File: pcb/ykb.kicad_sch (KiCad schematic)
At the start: 42 parts

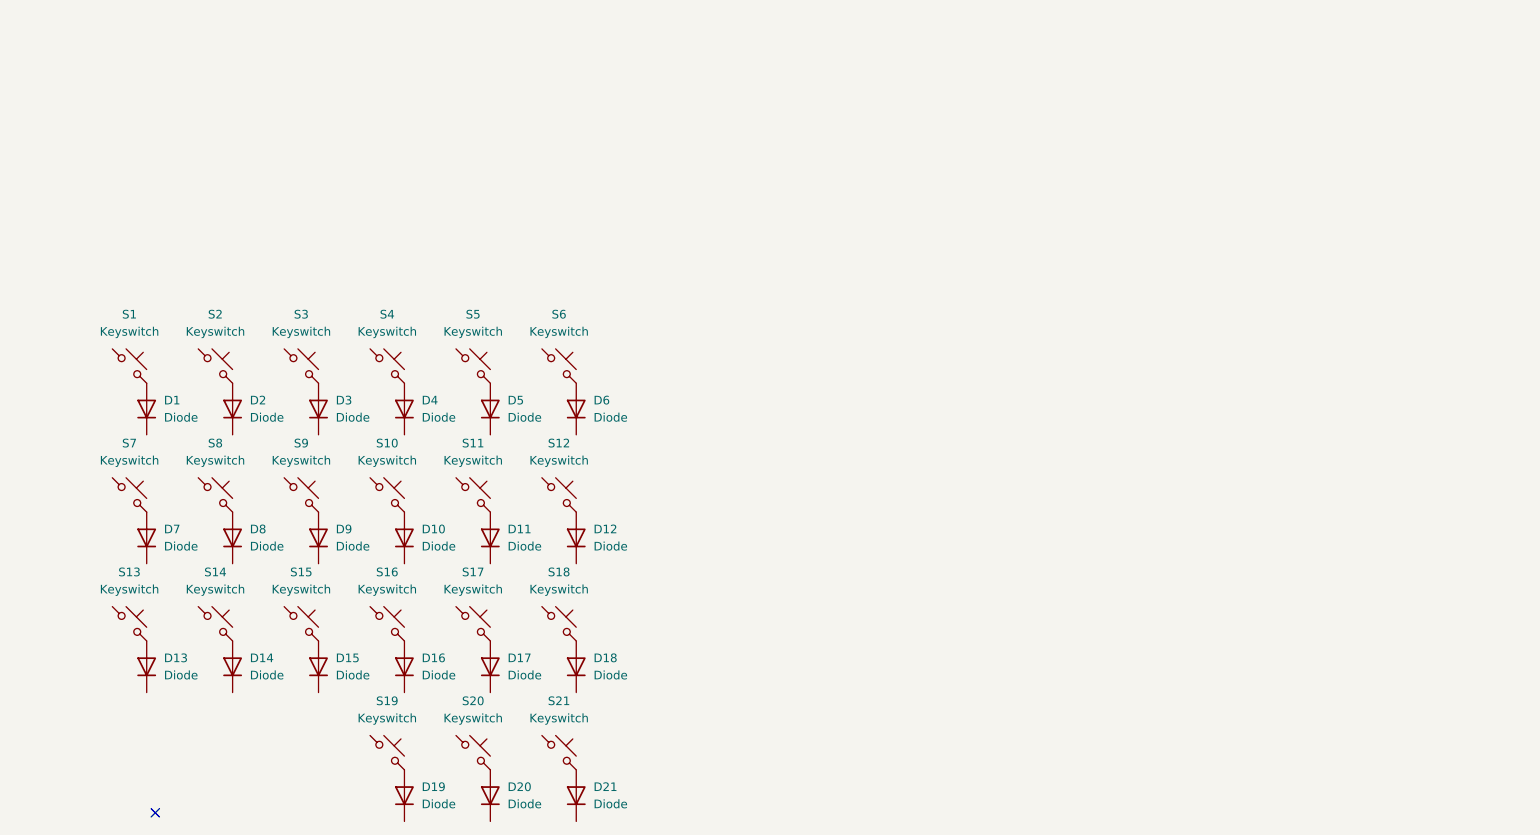
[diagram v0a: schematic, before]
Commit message: proper footprints and s/d connections made
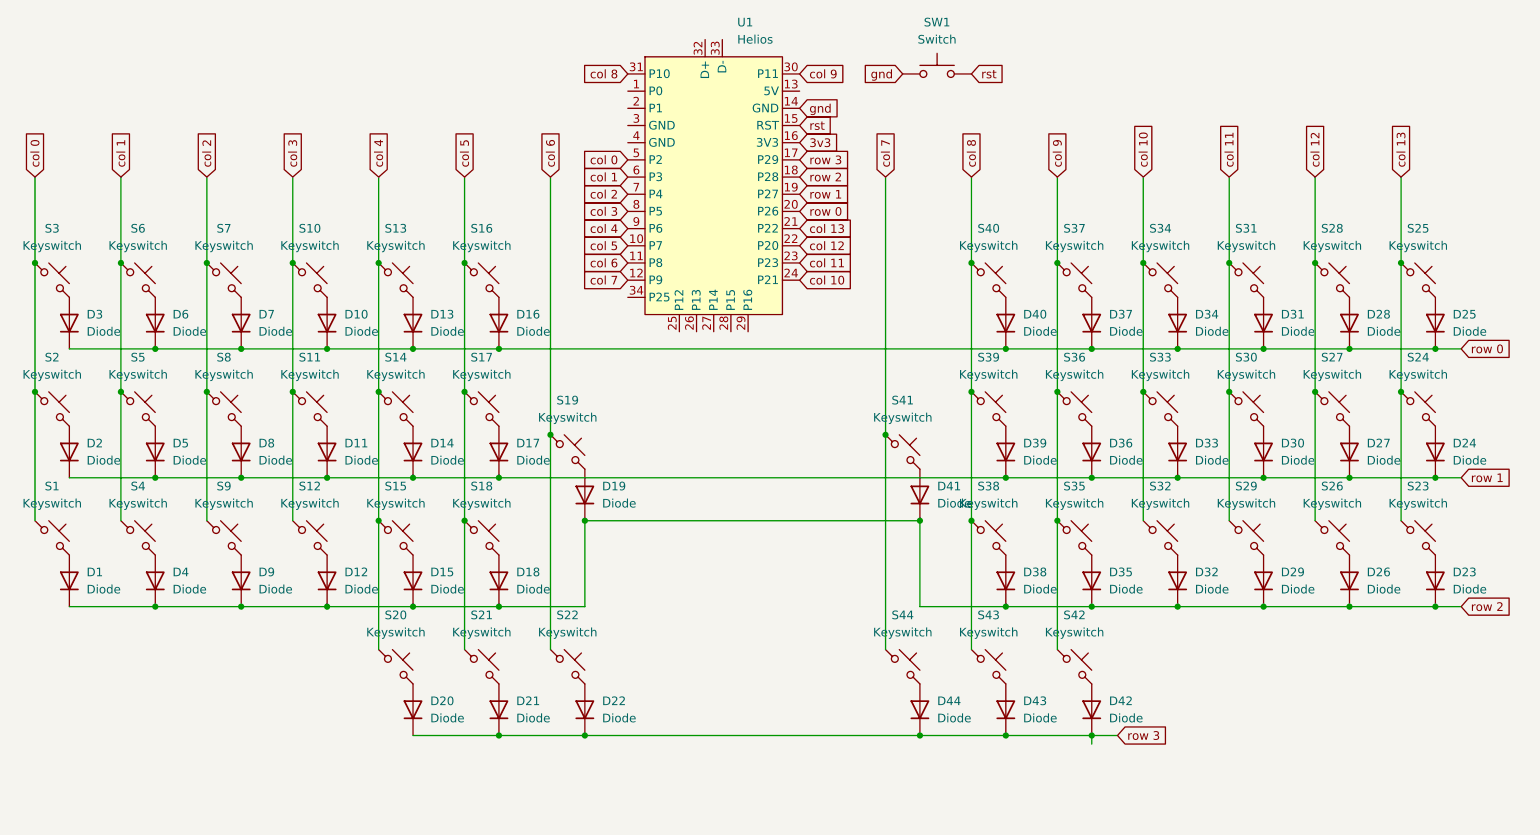
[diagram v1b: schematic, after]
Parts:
- added D22, D23, D24, D25, D26, D27, D28, D29, D30, D31, D32, D33, D34, D35, D36, D37, D38, D39, D40, D41, D42, D43, D44: Diode, ScottoKeebs_Components:Diode_SOD-123, symbol ScottoKeebs:Placeholder_Diode
- added S22, S23, S24, S25, S26, S27, S28, S29, S30, S31, S32, S33, S34, S35, S36, S37, S38, S39, S40, S41, S42, S43, S44: Keyswitch, ScottoKeebs_Hotswap:Hotswap_Choc_V1V2_1.00u, symbol ScottoKeebs:Placeholder_Keyswitch
- added SW1: Switch, ScottoKeebs_Components:Switch_MSK12C02, symbol ScottoKeebs:Placeholder_Switch
- added U1: Helios, PCM_marbastlib-xp-promicroish:Helios_AH_USBup, symbol PCM_marbastlib-promicroish:Helios
- D1, D10, D11, D12, D13, D14, D15, D16, D17, D18, D19, D2, D20, D21, D3, D4, D5, D6, D7, D8, D9: footprint (none) -> ScottoKeebs_Components:Diode_SOD-123
- S1, S10, S11, S12, S13, S14, S15, S16, S17, S18, S19, S2, S20, S21, S3, S4, S5, S6, S7, S8, S9: footprint (none) -> ScottoKeebs_Hotswap:Hotswap_Choc_V1V2_1.00u
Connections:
- net row 0: now reaches D7.1 (K)
- net row 0: now also D10.1 (K), D13.1 (K), D16.1 (K), D3.1 (K), D6.1 (K), D25.1 (K), D28.1 (K), D31.1 (K), D34.1 (K), D37.1 (K), D40.1 (K), U1.20 (P26)
- net col 3: now reaches S10.1
- net col 3: now also S11.1, S12.1, U1.8 (P5)
- net row 1: now reaches D14.1 (K)
- net row 1: now also D11.1 (K), D17.1 (K), D2.1 (K), D5.1 (K), D8.1 (K), D24.1 (K), D27.1 (K), D30.1 (K), D33.1 (K), D36.1 (K), D39.1 (K), U1.19 (P27)
- net row 2: now reaches D12.1 (K)
- net row 2: now also D1.1 (K), D15.1 (K), D18.1 (K), D19.1 (K), D4.1 (K), D9.1 (K), D23.1 (K), D26.1 (K), D29.1 (K), D32.1 (K), D35.1 (K), D38.1 (K), D41.1 (K), U1.18 (P28)
- net col 1: now reaches S6.1
- net col 1: now also S4.1, S5.1, U1.6 (P3)
- net col 6: now reaches S19.1
- net col 6: now also S22.1, U1.11 (P8)
- net col 2: now reaches S9.1
- net col 2: now also S7.1, S8.1, U1.7 (P4)
- net col 4: now reaches S15.1
- net col 4: now also S13.1, S14.1, S20.1, U1.9 (P6)
- net col 5: now reaches S17.1
- net col 5: now also S16.1, S18.1, S21.1, U1.10 (P7)
- net col 0: now reaches S1.1
- net col 0: now also S2.1, S3.1, U1.5 (P2)
- net row 3: now reaches D20.1 (K)
- net row 3: now also D21.1 (K), D22.1 (K), D42.1 (K), D43.1 (K), D44.1 (K), U1.17 (P29)
- new net: D23.2 (A), S23.2
- new net: D31.2 (A), S31.2
- new net: D39.2 (A), S39.2
- new net: D27.2 (A), S27.2
- new net: D41.2 (A), S41.2
- new net: D32.2 (A), S32.2
- new net: D36.2 (A), S36.2
- new net: D35.2 (A), S35.2
- new net: D28.2 (A), S28.2
- new net: D44.2 (A), S44.2
- new net: D38.2 (A), S38.2
- new net: D37.2 (A), S37.2
- new net: D22.2 (A), S22.2
- new net: D29.2 (A), S29.2
- new net: D40.2 (A), S40.2
- new net: D34.2 (A), S34.2
- new net: D42.2 (A), S42.2
- new net: D26.2 (A), S26.2
- new net: D24.2 (A), S24.2
- new net: D33.2 (A), S33.2
- new net: D25.2 (A), S25.2
- new net: D30.2 (A), S30.2
- new net: D43.2 (A), S43.2
- new net 3v3: U1.16 (3V3)
- new net col 10: S32.1, S33.1, S34.1, U1.24 (P21)
- new net col 11: S29.1, S30.1, S31.1, U1.23 (P23)
- new net col 12: S26.1, S27.1, S28.1, U1.22 (P20)
- new net col 13: S23.1, S24.1, S25.1, U1.21 (P22)
- new net col 7: S41.1, S44.1, U1.12 (P9)
- new net col 8: S38.1, S39.1, S40.1, S43.1, U1.31 (P10)
- new net col 9: S35.1, S36.1, S37.1, S42.1, U1.30 (P11)
- new net gnd: SW1.1, U1.14 (GND)
- new net rst: SW1.2, U1.15 (RST)
- no-connect marks 1 -> 0

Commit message: switched to castlated controller :3
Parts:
- U1: footprint PCM_marbastlib-xp-promicroish:Helios_AH_USBup -> PCM_marbastlib-xp-promicroish:Helios_AC
- renumbered D12 to D10, D10 to D12, D15 to D13, D13 to D15, D18 to D16, D16 to D18, D9 to D7, D7 to D9, S12 to S10, S10 to S12, S15 to S13, S13 to S15, S18 to S16, S16 to S18, S9 to S7, S7 to S9
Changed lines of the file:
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@@
 		(dnp no)
 		(fields_autoplaced yes)
-		(property "Reference" "S9"
+		(property "Reference" "S7"
 			(at 80.01 83.82 0)
 			(effects
@@
 			(project "ykb"
 				(path "/a72c5318-822d-41b0-b45a-b1b0853d4f62"
-					(reference "S9")
+					(reference "S7")
 					(unit 1)
 				)
@@
 		(dnp no)
 		(fields_autoplaced yes)
-		(property "Reference" "D7"
+		(property "Reference" "D9"
 			(at 85.09 58.4199 90)
 			(effects
@@
 			(project "ykb"
 				(path "/a72c5318-822d-41b0-b45a-b1b0853d4f62"
-					(reference "D7")
+					(reference "D9")
 					(unit 1)
 				)
@@
 		(dnp no)
 		(fields_autoplaced yes)
-		(property "Reference" "S18"
+		(property "Reference" "S16"
 			(at 118.11 83.82 0)
 			(effects
@@
 			(project "ykb"
 				(path "/a72c5318-822d-41b0-b45a-b1b0853d4f62"
-					(reference "S18")
+					(reference "S16")
 					(unit 1)
 				)
@@
 		(dnp no)
 		(fields_autoplaced yes)
-		(property "Reference" "S16"
+		(property "Reference" "S18"
 			(at 118.11 45.72 0)
 			(effects
@@
 			(project "ykb"
 				(path "/a72c5318-822d-41b0-b45a-b1b0853d4f62"
-					(reference "S16")
+					(reference "S18")
 					(unit 1)
 				)
@@
 		(dnp no)
 		(fields_autoplaced yes)
-		(property "Reference" "D16"
+		(property "Reference" "D18"
 			(at 123.19 58.4199 90)
 			(effects
@@
 			(project "ykb"
 				(path "/a72c5318-822d-41b0-b45a-b1b0853d4f62"
-					(reference "D16")
+					(reference "D18")
 					(unit 1)
 				)
@@
 		(on_board yes)
 		(dnp no)
-		(property "Reference" "D18"
+		(property "Reference" "D16"
 			(at 123.19 96.5199 90)
 			(effects
@@
 			(project "ykb"
 				(path "/a72c5318-822d-41b0-b45a-b1b0853d4f62"
-					(reference "D18")
+					(reference "D16")
 					(unit 1)
 				)
@@
 		(dnp no)
 		(fields_autoplaced yes)
-		(property "Reference" "S12"
+		(property "Reference" "S10"
 			(at 92.71 83.82 0)
 			(effects
@@
 			(project "ykb"
 				(path "/a72c5318-822d-41b0-b45a-b1b0853d4f62"
-					(reference "S12")
+					(reference "S10")
 					(unit 1)
 				)
@@
 		(dnp no)
 		(fields_autoplaced yes)
-		(property "Reference" "D9"
+		(property "Reference" "D7"
 			(at 85.09 96.5199 90)
 			(effects
@@
 			(project "ykb"
 				(path "/a72c5318-822d-41b0-b45a-b1b0853d4f62"
-					(reference "D9")
+					(reference "D7")
 					(unit 1)
 				)
@@
 		(dnp no)
 		(fields_autoplaced yes)
-		(property "Reference" "D13"
+		(property "Reference" "D15"
 			(at 110.49 58.4199 90)
 			(effects
@@
 			(project "ykb"
 				(path "/a72c5318-822d-41b0-b45a-b1b0853d4f62"
-					(reference "D13")
+					(reference "D15")
 					(unit 1)
 				)
@@
 		(dnp no)
 		(fields_autoplaced yes)
-		(property "Reference" "S13"
+		(property "Reference" "S15"
 			(at 105.41 45.72 0)
 			(effects
@@
 			(project "ykb"
 				(path "/a72c5318-822d-41b0-b45a-b1b0853d4f62"
-					(reference "S13")
+					(reference "S15")
 					(unit 1)
 				)
@@
 		(dnp no)
 		(fields_autoplaced yes)
-		(property "Reference" "D12"
+		(property "Reference" "D10"
 			(at 97.79 96.5199 90)
 			(effects
@@
 			(project "ykb"
 				(path "/a72c5318-822d-41b0-b45a-b1b0853d4f62"
-					(reference "D12")
+					(reference "D10")
 					(unit 1)
 				)
@@
 		(dnp no)
 		(fields_autoplaced yes)
-		(property "Reference" "S15"
+		(property "Reference" "S13"
 			(at 105.41 83.82 0)
 			(effects
@@
 			(project "ykb"
 				(path "/a72c5318-822d-41b0-b45a-b1b0853d4f62"
-					(reference "S15")
+					(reference "S13")
 					(unit 1)
 				)
@@
 		(dnp no)
 		(fields_autoplaced yes)
-		(property "Reference" "D10"
+		(property "Reference" "D12"
 			(at 97.79 58.4199 90)
 			(effects
@@
 			(project "ykb"
 				(path "/a72c5318-822d-41b0-b45a-b1b0853d4f62"
-					(reference "D10")
+					(reference "D12")
 					(unit 1)
 				)
@@
 		(dnp no)
 		(fields_autoplaced yes)
-		(property "Reference" "S7"
+		(property "Reference" "S9"
 			(at 80.01 45.72 0)
 			(effects
@@
 			(project "ykb"
 				(path "/a72c5318-822d-41b0-b45a-b1b0853d4f62"
-					(reference "S7")
+					(reference "S9")
 					(unit 1)
 				)
@@
 			)
 		)
-		(property "Footprint" "PCM_marbastlib-xp-promicroish:Helios_AH_USBup"
+		(property "Footprint" "PCM_marbastlib-xp-promicroish:Helios_AC"
 			(at 152.4 63.5 0)
 			(effects
@@
 		(dnp no)
 		(fields_autoplaced yes)
-		(property "Reference" "D15"
+		(property "Reference" "D13"
 			(at 110.49 96.5199 90)
 			(effects
@@
 			(project "ykb"
 				(path "/a72c5318-822d-41b0-b45a-b1b0853d4f62"
-					(reference "D15")
+					(reference "D13")
 					(unit 1)
 				)
@@
 		(dnp no)
 		(fields_autoplaced yes)
-		(property "Reference" "S10"
+		(property "Reference" "S12"
 			(at 92.71 45.72 0)
 			(effects
@@
 			(project "ykb"
 				(path "/a72c5318-822d-41b0-b45a-b1b0853d4f62"
-					(reference "S10")
+					(reference "S12")
 					(unit 1)
 				)

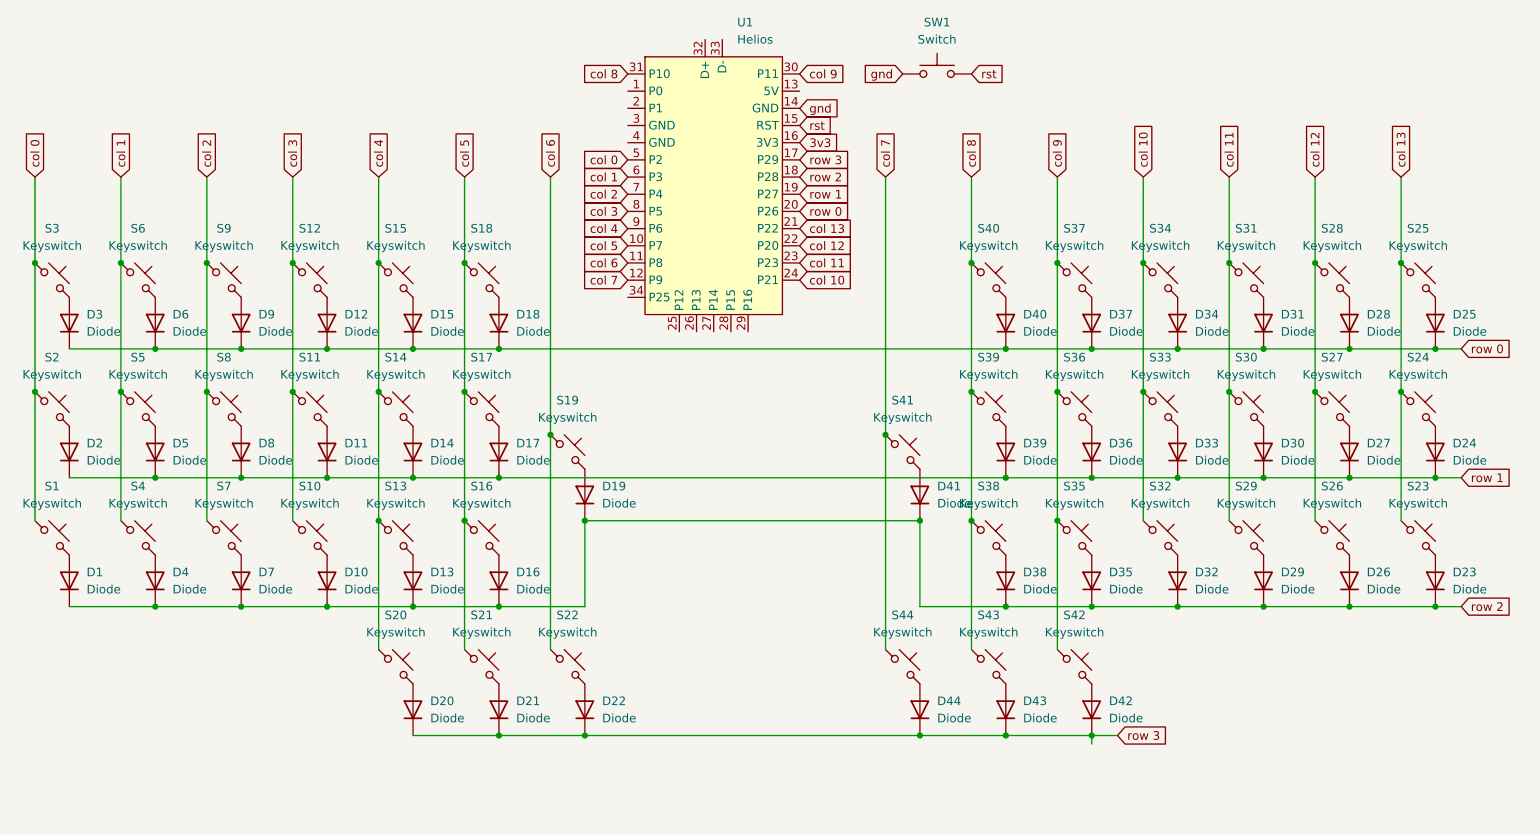
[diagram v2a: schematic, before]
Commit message: switched splay from key units to degrees because i did key units for some reason
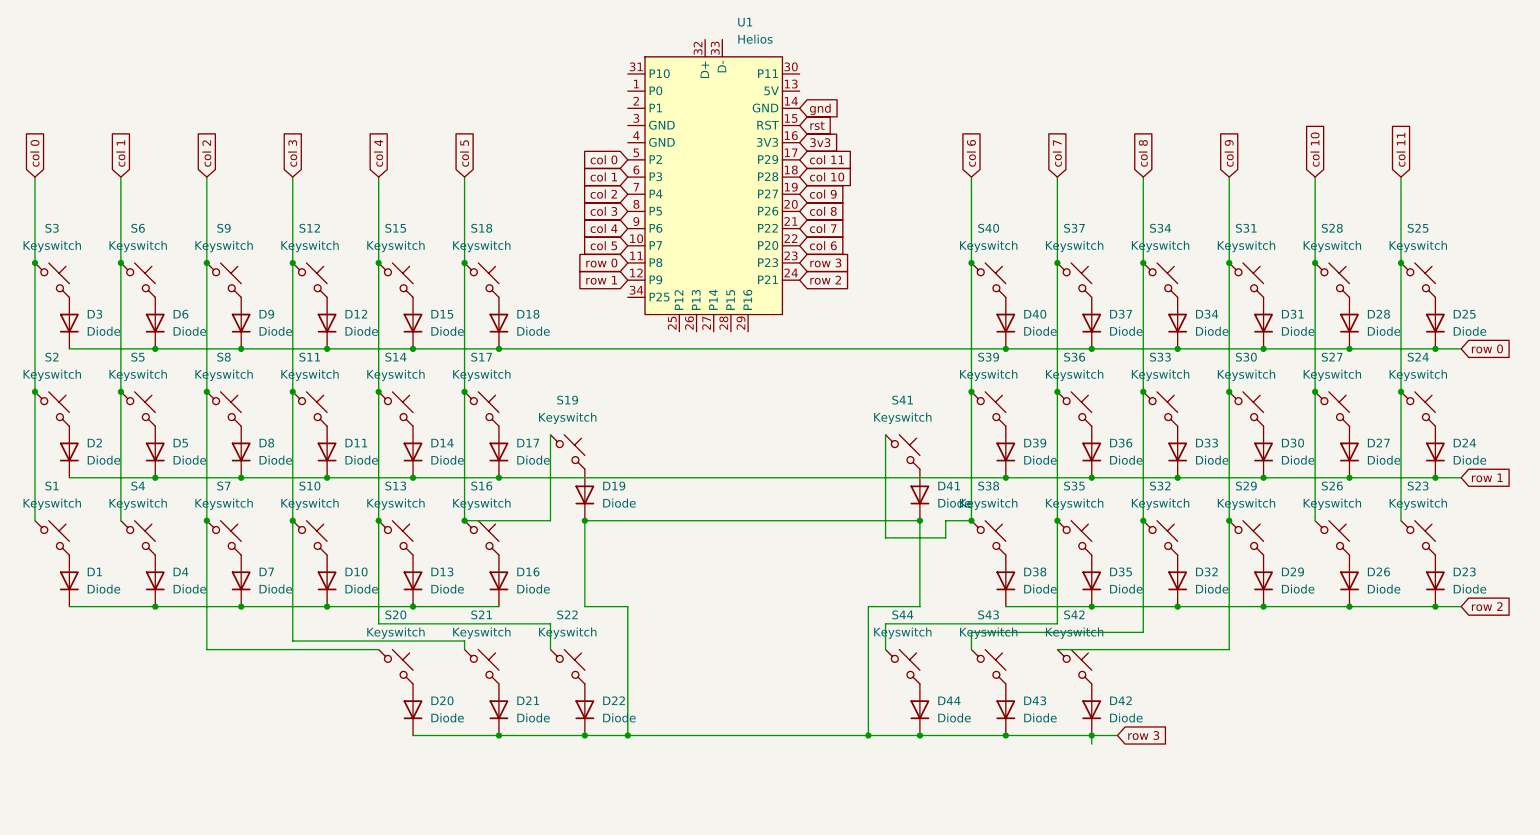
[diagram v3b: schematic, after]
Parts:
- removed SW1: Switch, ScottoKeebs_Components:Switch_MSK12C02, symbol ScottoKeebs:Placeholder_Switch
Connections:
- net col 10: now also S26.1, S27.1, S28.1, U1.18 (P28); no longer S32.1, S33.1, S34.1, U1.24 (P21)
- net col 11: now also S23.1, S24.1, S25.1, U1.17 (P29); no longer S29.1, S30.1, S31.1, U1.23 (P23)
- net col 2: now also S20.1
- net col 3: now also S21.1
- net col 4: now also S22.1; no longer S20.1
- net col 5: now also S19.1; no longer S21.1
- net col 6: now also S38.1, S39.1, S40.1, S41.1, U1.22 (P20); no longer S19.1, S22.1, U1.11 (P8)
- net col 7: now also S35.1, S36.1, S37.1, U1.21 (P22); no longer S41.1, U1.12 (P9)
- net col 8: now also S32.1, S33.1, S34.1, U1.20 (P26); no longer S38.1, S39.1, S40.1, U1.31 (P10)
- net col 9: now also S29.1, S30.1, S31.1, U1.19 (P27); no longer S35.1, S36.1, S37.1, U1.30 (P11)
- net row 0: now also U1.11 (P8); no longer U1.20 (P26)
- net row 1: now also U1.12 (P9); no longer U1.19 (P27)
- net row 2: now also U1.24 (P21); no longer D1.1 (K), D10.1 (K), D13.1 (K), D16.1 (K), D19.1 (K), D4.1 (K), D41.1 (K), D7.1 (K), U1.18 (P28)
- net row 3: now also D19.1 (K), D41.1 (K), U1.23 (P23); no longer U1.17 (P29)
- removed net col 12: S26.1, S27.1, S28.1, U1.22 (P20)
- removed net col 13: S23.1, S24.1, S25.1, U1.21 (P22)
- new net: D1.1 (K), D10.1 (K), D13.1 (K), D16.1 (K), D4.1 (K), D7.1 (K)
